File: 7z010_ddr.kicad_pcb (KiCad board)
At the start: 4 copper layers, 51 parts, among them U1 DDR3, U2 xc7z010clg400

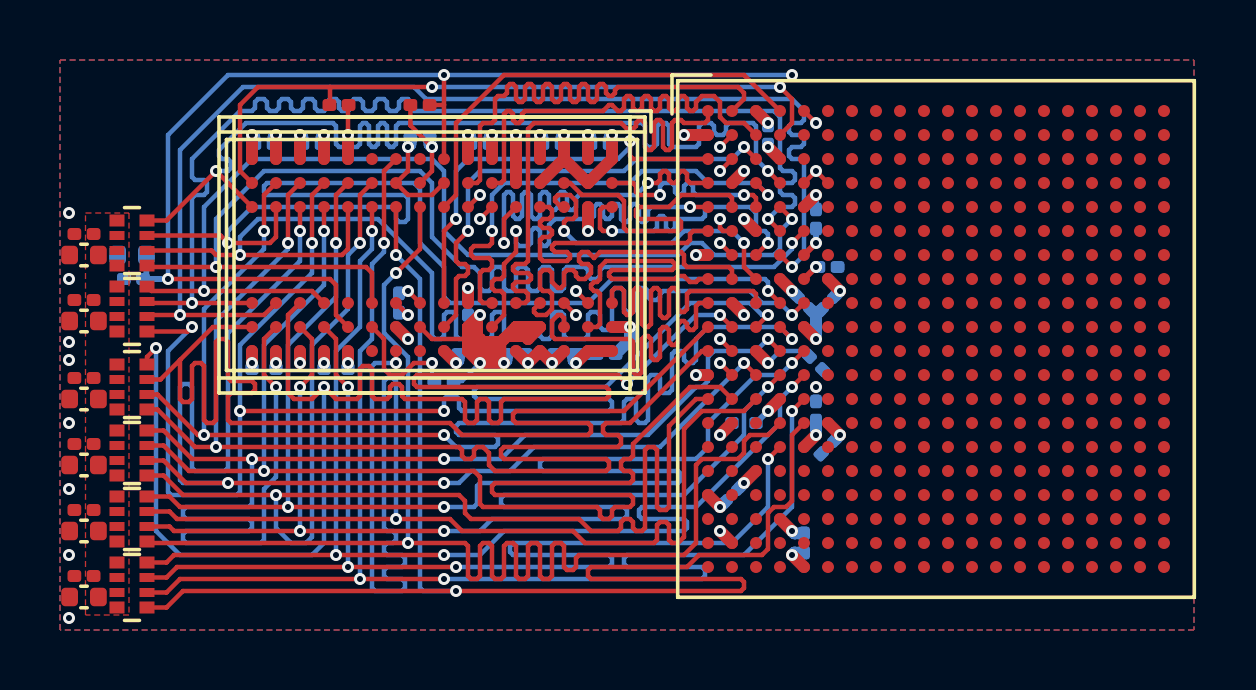
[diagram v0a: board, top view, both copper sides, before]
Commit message: added GND back to sch
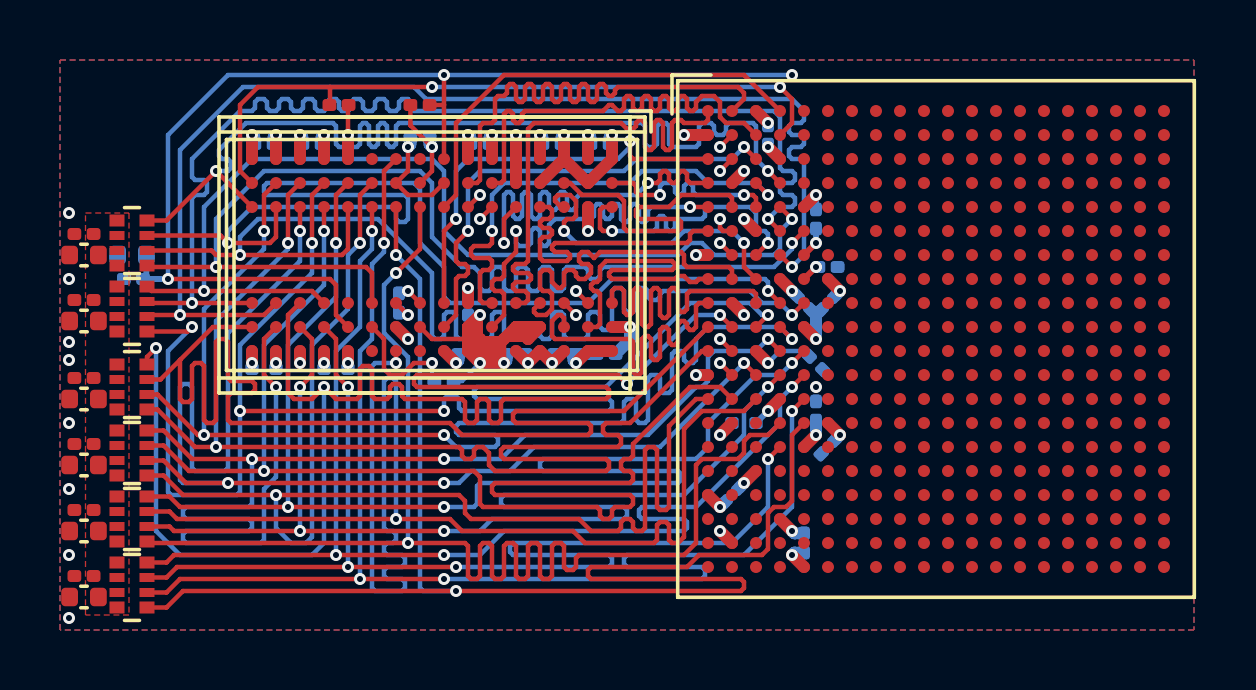
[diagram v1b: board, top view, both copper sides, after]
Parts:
- R1, R4, R5: value 100Ω -> 80Ω
- RN1, RN2, RN3, RN4, RN5, RN6: value 50Ω -> 40Ω
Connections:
- U2 pad A18: (no net) -> GND
- U2 pad A8: (no net) -> GND
- U2 pad B1: (no net) -> GND
- U2 pad B11: (no net) -> GND
- U2 pad C14: (no net) -> GND
- U2 pad C4: (no net) -> GND
- U2 pad C9: (no net) -> GND
- U2 pad D17: (no net) -> GND
- U2 pad E10: (no net) -> GND
- U2 pad E20: (no net) -> GND
- U2 pad F3: (no net) -> GND
- U2 pad F7: (no net) -> GND
- U2 pad F8: (no net) -> Net-(U2-PadF8)
- U2 pad G10: (no net) -> GND
- U2 pad G11: (no net) -> Net-(U2-PadG11)
- U2 pad G12: (no net) -> GND
- U2 pad G13: (no net) -> Net-(U2-PadG13)
- U2 pad G16: (no net) -> GND
- U2 pad G7: (no net) -> Net-(U2-PadG7)
- U2 pad G9: (no net) -> Net-(U2-PadF8)
- U2 pad H10: (no net) -> Net-(U2-PadG11)
- U2 pad H11: (no net) -> GND
- U2 pad H12: (no net) -> Net-(U2-PadG13)
- U2 pad H13: (no net) -> GND
- U2 pad H19: (no net) -> GND
- U2 pad H7: (no net) -> GND
- U2 pad H8: (no net) -> Net-(U2-PadF8)
- U2 pad H9: (no net) -> GND
- U2 pad J11: (no net) -> Net-(U2-PadJ11)
- U2 pad J12: (no net) -> GND
- U2 pad J13: (no net) -> Net-(U2-PadG13)
- U2 pad J2: (no net) -> GND
- U2 pad J7: (no net) -> Net-(U2-PadG7)
- U2 pad J8: (no net) -> GND
- U2 pad K11: (no net) -> GND
- U2 pad K12: (no net) -> Net-(U2-PadG13)
- U2 pad K13: (no net) -> GND
- U2 pad K15: (no net) -> GND
- U2 pad K5: (no net) -> GND
- U2 pad K7: (no net) -> GND
- U2 pad K8: (no net) -> Net-(U2-PadF8)
- U2 pad L11: (no net) -> Net-(U2-PadJ11)
- U2 pad L12: (no net) -> GND
- U2 pad L13: (no net) -> Net-(U2-PadG13)
- U2 pad L18: (no net) -> GND
- U2 pad L7: (no net) -> Net-(U2-PadG7)
- U2 pad L8: (no net) -> GND
- U2 pad M1: (no net) -> GND
- U2 pad M11: (no net) -> GND
- U2 pad M12: (no net) -> Net-(U2-PadG13)
- U2 pad M13: (no net) -> GND
- U2 pad M7: (no net) -> GND
- U2 pad M8: (no net) -> Net-(U2-PadF8)
- U2 pad N10: (no net) -> GND
- U2 pad N11: (no net) -> Net-(U2-PadJ11)
- U2 pad N12: (no net) -> GND
- U2 pad N13: (no net) -> Net-(U2-PadG13)
- U2 pad N14: (no net) -> GND
- U2 pad N4: (no net) -> GND
- U2 pad N7: (no net) -> Net-(U2-PadG7)
- U2 pad N8: (no net) -> GND
- U2 pad N9: (no net) -> Net-(U2-PadJ11)
- U2 pad P10: (no net) -> Net-(U2-PadJ11)
- U2 pad P11: (no net) -> GND
- U2 pad P12: (no net) -> Net-(U2-PadG13)
- U2 pad P13: (no net) -> GND
- U2 pad P17: (no net) -> GND
- U2 pad P7: (no net) -> GND
- U2 pad P8: (no net) -> Net-(U2-PadG7)
- U2 pad P9: (no net) -> GND
- U2 pad R12: (no net) -> GND
- U2 pad R13: (no net) -> Net-(U2-PadG13)
- U2 pad R20: (no net) -> GND
- U2 pad R7: (no net) -> Net-(U2-PadG7)
- U2 pad R8: (no net) -> GND
- U2 pad R9: (no net) -> Net-(U2-PadJ11)
- U2 pad T13: (no net) -> GND
- U2 pad T3: (no net) -> GND
- U2 pad T7: (no net) -> GND
- U2 pad U16: (no net) -> GND
- U2 pad U6: (no net) -> GND
- U2 pad V19: (no net) -> GND
- U2 pad V9: (no net) -> GND
- U2 pad W12: (no net) -> GND
- U2 pad W2: (no net) -> GND
- U2 pad Y15: (no net) -> GND
- U2 pad Y5: (no net) -> GND
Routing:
- net (no net): track 4.59 -> 0.00 mm, vias 7 -> 0
- net GND: track 42.3 -> 45.2 mm, vias 30 -> 35
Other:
- board text added: "GNU GPL"
